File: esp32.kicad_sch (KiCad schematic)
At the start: 10 parts, among them J2 TC2030-IDC, J3 Conn_01x04, J4 Conn_01x08, J5 USB_C_Receptacle_USB2.0, SW1 SWITCH-SPST, SW2 SWITCH-SPST, U5 ESP32-S3-WROOM-1

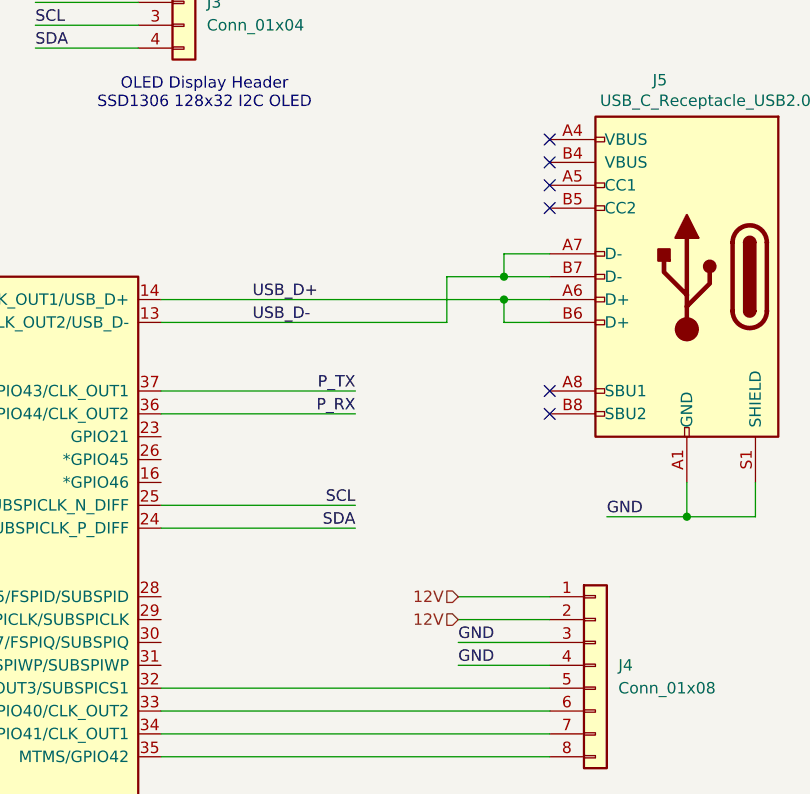
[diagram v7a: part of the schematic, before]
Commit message: routing is done. Power planes look good. DRC pass
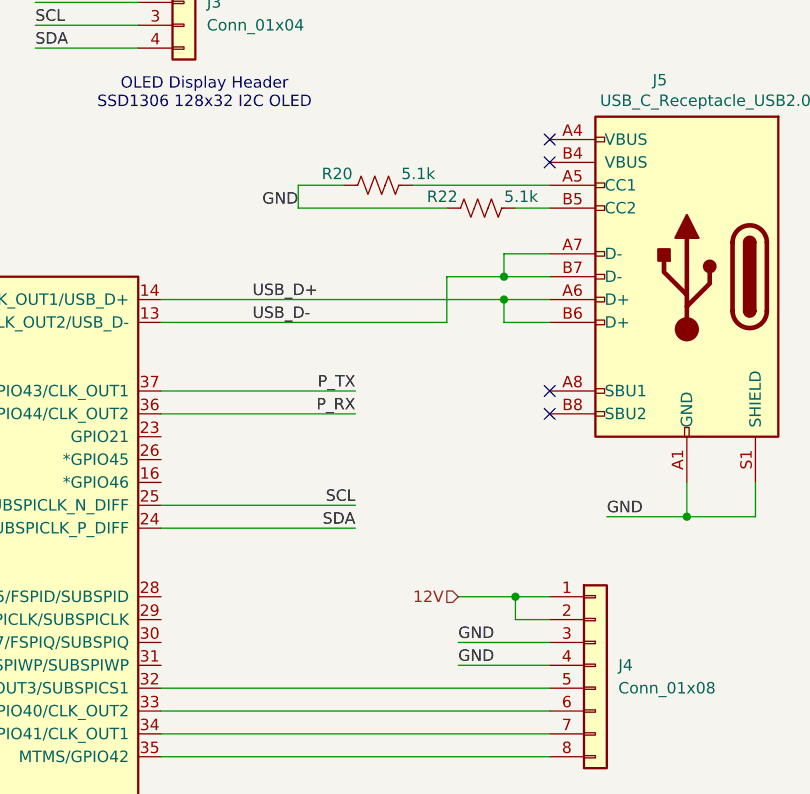
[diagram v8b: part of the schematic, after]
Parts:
- added R20, R22: 5.1k, Resistor_SMD:R_0402_1005Metric, symbol Device:R_US
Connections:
- net GND: now also R20.1, R22.1
- net at J5.A5 (CC1): now also R20.2
- net at J5.B5 (CC2): now also R22.2
- no-connect marks 6 -> 4
